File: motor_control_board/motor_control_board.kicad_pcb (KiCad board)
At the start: 4 copper layers, 45 x 40 mm, 78 parts, among them J1 Conn_01x05_Female, J2 Conn_01x05_Female, J3 Harwin_G125-MG10605M4P, J4 Harwin_M80-5000000M5-02-333-0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, J5 Harwin_M80-5400642, J6 Harwin_M80-8510442, J7 Harwin_M80-8510442, Q1 ECH8420-TL-H, U1 CPC1117N, U2 MCP2562, U3 PIC18F26K83, U4 MCP2562, U5 PIC18F26K83, U6 SN74LVC1G14DBV, U7 INA232AIDDFR, U8 UA78M05IDCYR, X1 12MHz, X2 12MHz

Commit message: PCB routing 70% done
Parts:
- removed Q1: ECH8420-TL-H, Package_TO_SOT_SMD:OnSemi_ECH8
- added U9: ECH8420-TL-H, Package_TO_SOT_SMD:OnSemi_ECH8, B.Cu at (180.6, 60.3)
- moved R23 2.34 mm to (186.4, 60.1)
- moved R10 2.14 mm to (181.1, 72.7)
- moved R9 1.78 mm to (181.1, 70.7)
- moved R24 1.65 mm to (184.3, 60.1)
- moved F2 0.54 mm to (172.4, 94.4)
- moved R5 0.48 mm to (168.7, 67.8)
- moved D1 0.41 mm to (177.7, 94.5)
- moved C7 0.32 mm to (164.9, 82.7)
- moved R20 0.23 mm to (171.5, 74.4)
- moved R25 0.23 mm to (169.6, 74.4)
- moved R21 0.23 mm to (173.4, 74.4)
- moved C5 0.20 mm to (181.1, 68.7)
- moved R4 0.15 mm to (164.6, 67.8)
- moved C13 0.08 mm to (163.2, 74.7)
- moved C2 0.08 mm to (186.4, 82.8)
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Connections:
- F2 pad 1: +12V -> /Batt+
- U5 pad 21: /ENC1 -> unconnected-(U5-RB0-Pad21)
- U5 pad 4: unconnected-(U5-RA2-Pad4) -> /ENC1
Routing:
- net /ICSPCLK_FS: track 0.00 -> 46.5 mm, vias 0 -> 1
- net /ICSPDAT_FS: track 0.00 -> 40.0 mm, vias 0 -> 1
- net Net-(U5-~{MCLR}): track 0.00 -> 27.1 mm, vias 0 -> 1
- net /ENC1: track 0.00 -> 19.5 mm
- net /Failsafe MCU/SDA_FS: track 0.00 -> 18.0 mm, vias 0 -> 1
- net /ALERT: track 0.00 -> 17.4 mm, vias 0 -> 1
- net /ENC2: track 0.00 -> 13.7 mm
- net GND: track 0.00 -> 13.7 mm, vias 0 -> 15
- net /Failsafe MCU/SCL_FS: track 0.00 -> 12.7 mm, vias 0 -> 1
- net Net-(U3-~{MCLR}): track 0.00 -> 11.8 mm, vias 0 -> 1
- net /MCLR_MCU: track 0.00 -> 11.5 mm
- net /MCLR_FS: track 0.00 -> 11.0 mm
- net /ICSPDAT_MCU: track 0.00 -> 9.90 mm, vias 0 -> 1
- net +5V: track 0.00 -> 9.66 mm, vias 0 -> 4
- net /ICSPCLK_MCU: track 0.00 -> 7.63 mm, vias 0 -> 1
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- added copper zone on B.Cu, net +12V
- added copper zone on In2.Cu, net +5V
- added copper zone on B.Cu, net /Batt+
- added copper zone on B.Cu, net /Servo+
- added copper zone on B.Cu, net /Servo-
- added copper zone on B.Cu, net GND
- added copper zone on F.Cu, net GND
- added copper zone on In1.Cu, net GND

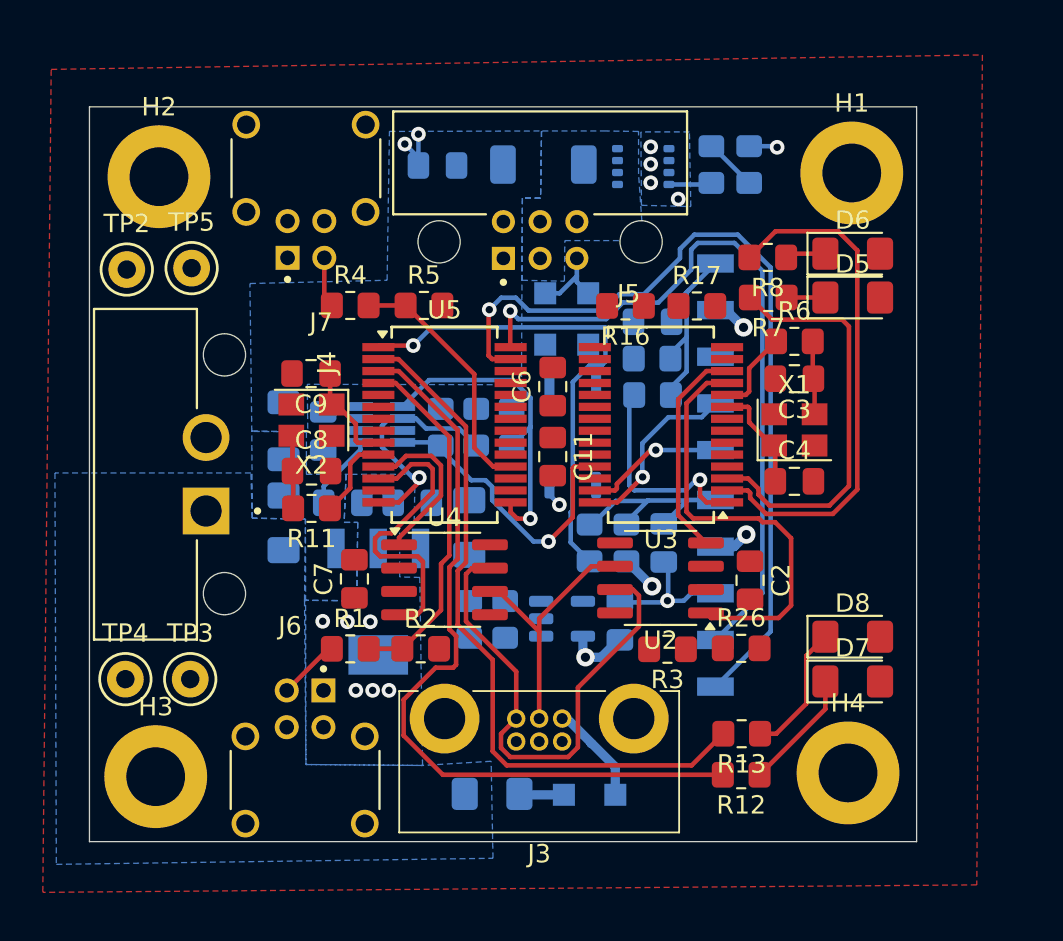
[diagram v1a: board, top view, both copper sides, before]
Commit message: Routing Complete
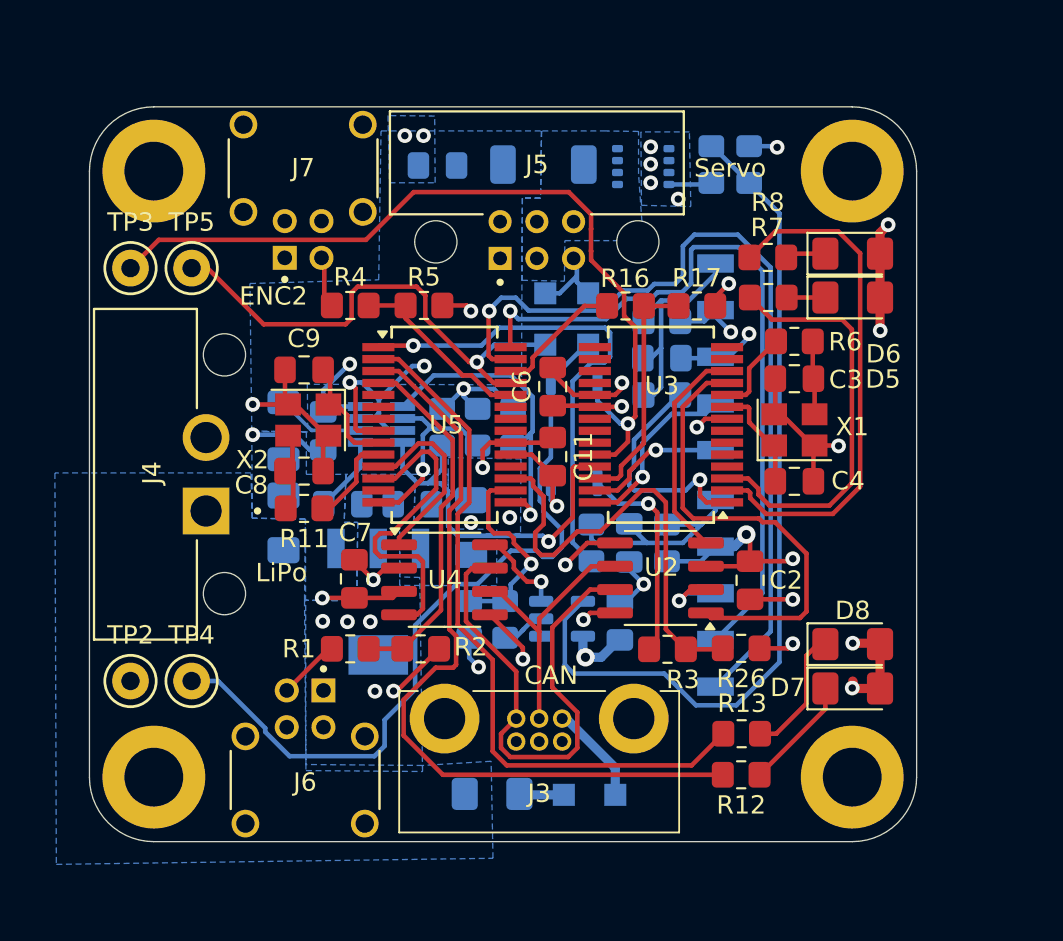
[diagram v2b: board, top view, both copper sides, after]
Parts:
- moved TP3 22.6 mm to (152.7, 65.8)
- moved TP2 22.4 mm to (152.7, 88.3)
- moved TP4 3.61 mm to (156.0, 88.3)
- moved R14 2.21 mm to (181.9, 80.7)
- moved R9 2.10 mm to (181.6, 68.7), turned to 180 degrees
- moved C5 2.05 mm to (181.6, 70.7), turned to 0 degrees
- moved C10 1.88 mm to (179.8, 80.7)
- moved R10 0.51 mm to (181.6, 72.7), turned to 180 degrees
- moved C9 0.43 mm to (162.1, 71.3)
- moved H2 0.41 mm to (153.9, 60.5)
- moved C8 0.41 mm to (162.1, 76.8)
- moved R11 0.41 mm to (162.1, 78.9)
- moved D8 0.41 mm to (192.0, 86.3)
- moved D7 0.38 mm to (192.0, 88.7)
- moved H4 0.32 mm to (192.0, 93.5)
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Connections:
- net Net-(U8-OUTPUT) renamed /Power/LDO_OUT
- U5 pad 16: unconnected-(U5-RC5-Pad16) -> /Failsafe MCU/FET
- U5 pad 17: unconnected-(U5-RC6-Pad17) -> /FS_OVER
- U5 pad 18: /ENC2 -> unconnected-(U5-RC7-Pad18)
- U5 pad 22: /Failsafe MCU/FET -> unconnected-(U5-RB1-Pad22)
- U5 pad 23: /FS_OVER -> unconnected-(U5-RB2-Pad23)
- U5 pad 24: /PWM_FS -> /ENC2
- U5 pad 25: unconnected-(U5-RB4-Pad25) -> /PWM_FS
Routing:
- net GND: track 13.7 -> 83.1 mm, vias 15 -> 31
- net +5V: track 9.66 -> 62.3 mm, vias 4 -> 17
- net /PWM_MCU: track 0.00 -> 46.2 mm, vias 0 -> 1
- net Net-(R23-Pad1): track 2.89 -> 47.1 mm
- net /PWM_SERVO: track 0.00 -> 42.4 mm
- net /PWM_FS: track 0.00 -> 27.4 mm, vias 0 -> 1
- net /FS_OVER: track 0.00 -> 24.9 mm
- net /Failsafe MCU/FS_MCU: track 0.00 -> 13.1 mm
- net Net-(R3-Pad2): track 0.00 -> 11.6 mm, vias 0 -> 1
- net /Failsafe MCU/FET: track 0.00 -> 11.1 mm, vias 0 -> 1
- net Net-(U5-RB5): track 0.00 -> 7.01 mm
- net /Servo+: track 0.00 -> 4.82 mm
- net /ALERT: track 17.4 -> 21.6 mm
- net /ENC2: track 13.7 -> 10.2 mm
- net Net-(R19-Pad2): track 0.00 -> 2.40 mm
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- added copper zone on B.Cu, net +5V
- added copper zone on B.Cu, net /Power/LDO_OUT
- removed copper zone on F.Cu, net GND
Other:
- outline, holes or cut-outs redrawn
- board text added: "CAN"
- board text added: "ENC2"
- board text added: "FS"
- board text added: "LiPo"
- board text added: "MCU"
- board text added: "Servo"

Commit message: Silkscreen and minor copper pour edits
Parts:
- renumbered TP2 to +5V, TP5 to PWM_F, TP3 to PWM_M, TP4 to PWM_S
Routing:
- net GND: vias 31 -> 44
- added copper zone on F.Cu, net GND
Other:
- board text added: "ENC1"

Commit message: Fixed symbol and footprint libraries
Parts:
- +5V, PWM_F, PWM_M, PWM_S: footprint TestPoint:TestPoint_Keystone_5000-5004_Miniature -> canhw_footprints:TestPoint_Keystone_5000-5004_Miniature
- C1, C10, C11, C12, C13, C14, C15, C2, C3, C4, C5, C6, C7, C8, C9: footprint Capacitor_SMD:C_0805_2012Metric_Pad1.18x1.45mm_HandSolder -> canhw_footprints:C_0805_2012Metric_Pad1.18x1.45mm_HandSolder
- D1, D2, D3: footprint Diode_SMD:Nexperia_CFP3_SOD-123W -> canhw_footprints:Nexperia_CFP3_SOD-123W
- D4: footprint Diode_SMD:D_SOD-128 -> canhw_footprints:D_SOD-128
- D5, D6, D7, D8: footprint LED_SMD:LED_1206_3216Metric_Pad1.42x1.75mm_HandSolder -> canhw_footprints:LED_1206_3216Metric_Pad1.42x1.75mm_HandSolder
- F1, F2, F3: footprint Fuse:Fuse_1206_3216Metric_Pad1.42x1.75mm_HandSolder -> canhw_footprints:Fuse_1206_3216Metric_Pad1.42x1.75mm_HandSolder
- H1, H2, H3, H4: footprint MountingHole:MountingHole_3.2mm_M3_DIN965_Pad -> canhw_footprints:MountingHole_3.2mm_M3_DIN965_Pad
- J4: footprint motor-control:HARWIN_M80-5000000M5-02-333-00-000 -> canhw_footprints:HARWIN_M80-5000000M5-02-333-00-000
- J5: footprint motor-control:HARWIN_M80-5400642 -> canhw_footprints:HARWIN_M80-5400642
- J6, J7: footprint motor-control:HARWIN_M80-8510442 -> canhw_footprints:HARWIN_M80-8510442
- R1, R10, R11, R12, R13, R14, R15, R16, R17, R18, R19, R2, R20, R21, R23, R24, R25, R26, R3, R4, R5, R6, R7, R8, R9: footprint Resistor_SMD:R_0805_2012Metric_Pad1.20x1.40mm_HandSolder -> canhw_footprints:R_0805_2012Metric_Pad1.20x1.40mm_HandSolder
- R22: footprint Resistor_SMD:R_1206_3216Metric_Pad1.30x1.75mm_HandSolder -> canhw_footprints:R_1206_3216Metric_Pad1.30x1.75mm_HandSolder
- U1: footprint Package_SO:SOP-4_3.8x4.1mm_P2.54mm -> canhw_footprints:SOP-4_3.8x4.1mm_P2.54mm
- U2, U4: footprint Package_SO:SOIC-8_3.9x4.9mm_P1.27mm -> canhw_footprints:SOIC-8_3.9x4.9mm_P1.27mm
- U3, U5: footprint Package_SO:SSOP-28_5.3x10.2mm_P0.65mm -> canhw_footprints:SSOP-28_5.3x10.2mm_P0.65mm
- U6: footprint Package_TO_SOT_SMD:SOT-23-5 -> canhw_footprints:SOT-23-5
- U7: footprint motor-control:SOT65P280X110-8N -> canhw_footprints:SOT65P280X110-8N
- U8: footprint motor-control:SOT230P700X180-4N -> canhw_footprints:SOT230P700X180-4N
- U9: footprint Package_TO_SOT_SMD:OnSemi_ECH8 -> canhw_footprints:OnSemi_ECH8
- X1, X2: footprint Crystal:Crystal_SMD_Abracon_ABM8G-4Pin_3.2x2.5mm -> canhw_footprints:Crystal_SMD_Abracon_ABM8G-4Pin_3.2x2.5mm

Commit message: minor touchups
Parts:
- added G***: LOGO, Team_Logo:Logo_SilkScreen_5mm, F.Cu at (191.9, 80.5)
- added G***: LOGO, Team_Logo:Logo_SilkScreen_5mm, B.Cu at (169.8, 68.1)
- renumbered +5V to 5V, PWM_F to FS, PWM_M to MCU, PWM_S to PWM
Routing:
- net GND: track 83.1 -> 84.4 mm
- net Net-(U5-~{MCLR}): track 27.3 -> 28.0 mm
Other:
- board text added: "Board"
- board text added: "J. Huang"
- board text added: "Missile Control"
- board text added: "PWM"

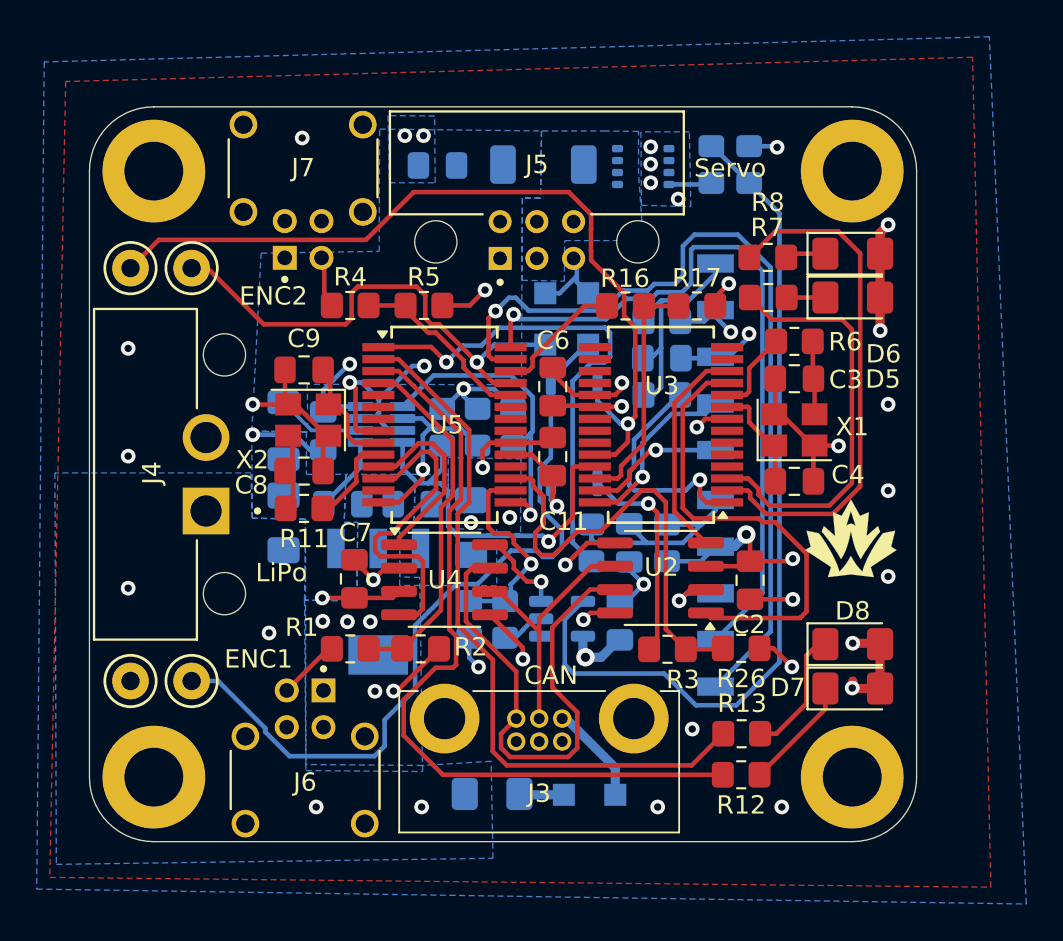
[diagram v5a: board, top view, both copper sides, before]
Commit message: Fixed DRC errors except for the PTH keep out zones
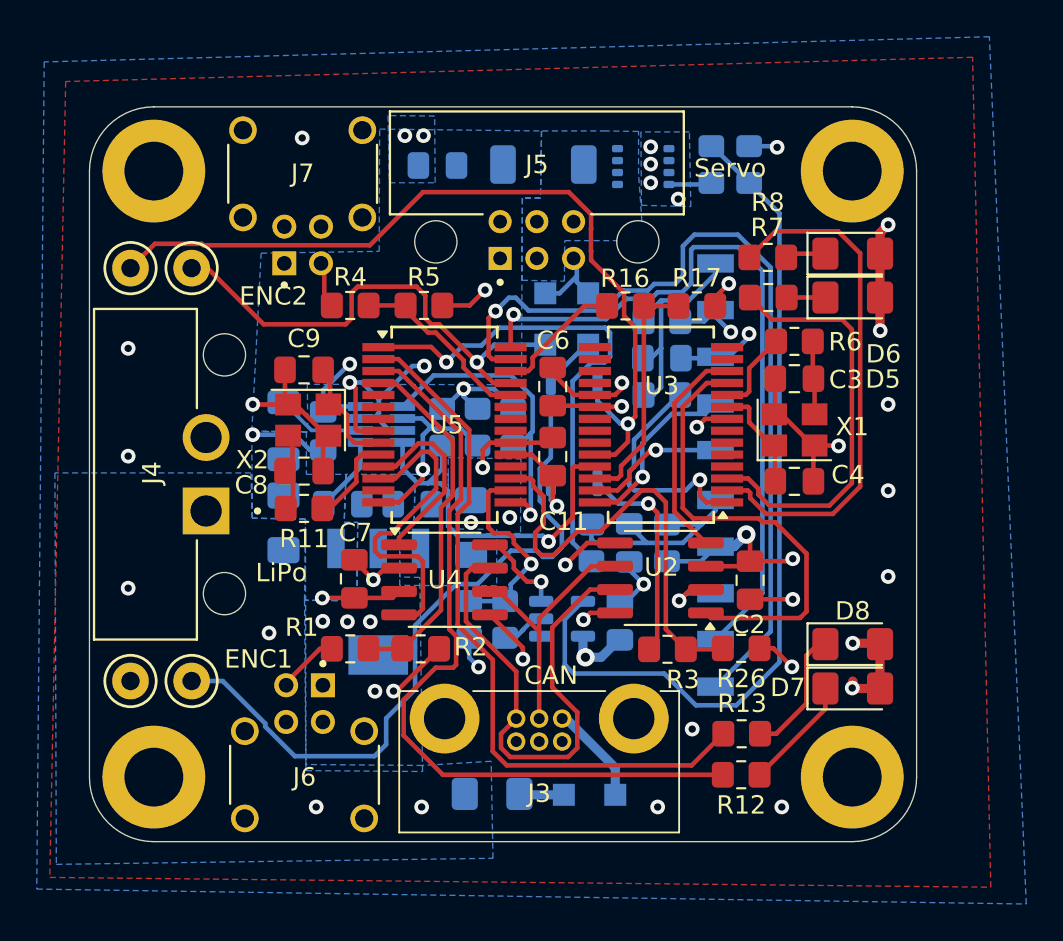
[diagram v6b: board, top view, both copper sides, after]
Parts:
- removed G*** (x2): LOGO, Team_Logo:Logo_SilkScreen_5mm
- moved J7 0.30 mm to (162.1, 60.7)
- moved J6 0.29 mm to (162.2, 93.4)
- renumbered 5V to TP2, MCU to TP3, PWM to TP4, FS to TP5
